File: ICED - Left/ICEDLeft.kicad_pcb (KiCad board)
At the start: 2 copper layers, 175.4 x 145 mm, 162 parts, among them P1 Conn_ARM_JTAG_SWD_10, P2 DX07S024XJ1R1100, P3 CONN_17, P4 692121130100, P5 RGB Out, Q1 TC1264, U1 MK20DX256VLH7, U2 IS31FL3737-QFLS4-TR, X1 CRYSTAL

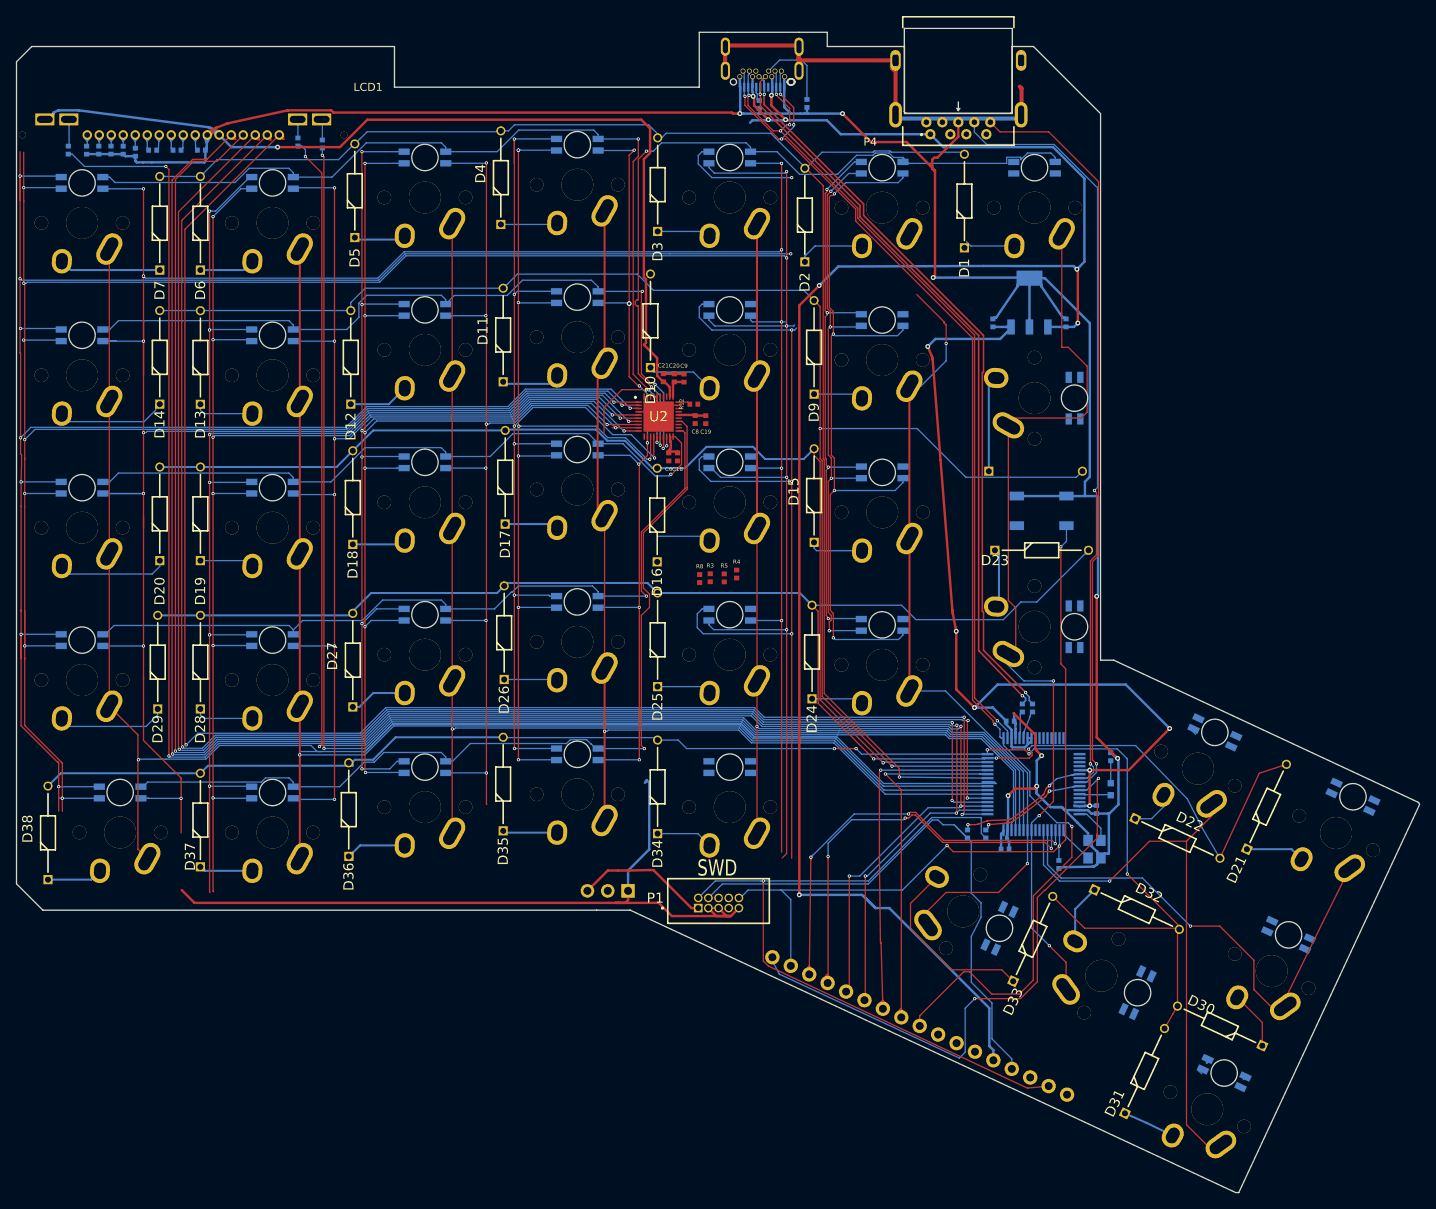
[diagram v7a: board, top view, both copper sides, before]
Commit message: Cleaned up DRC issues
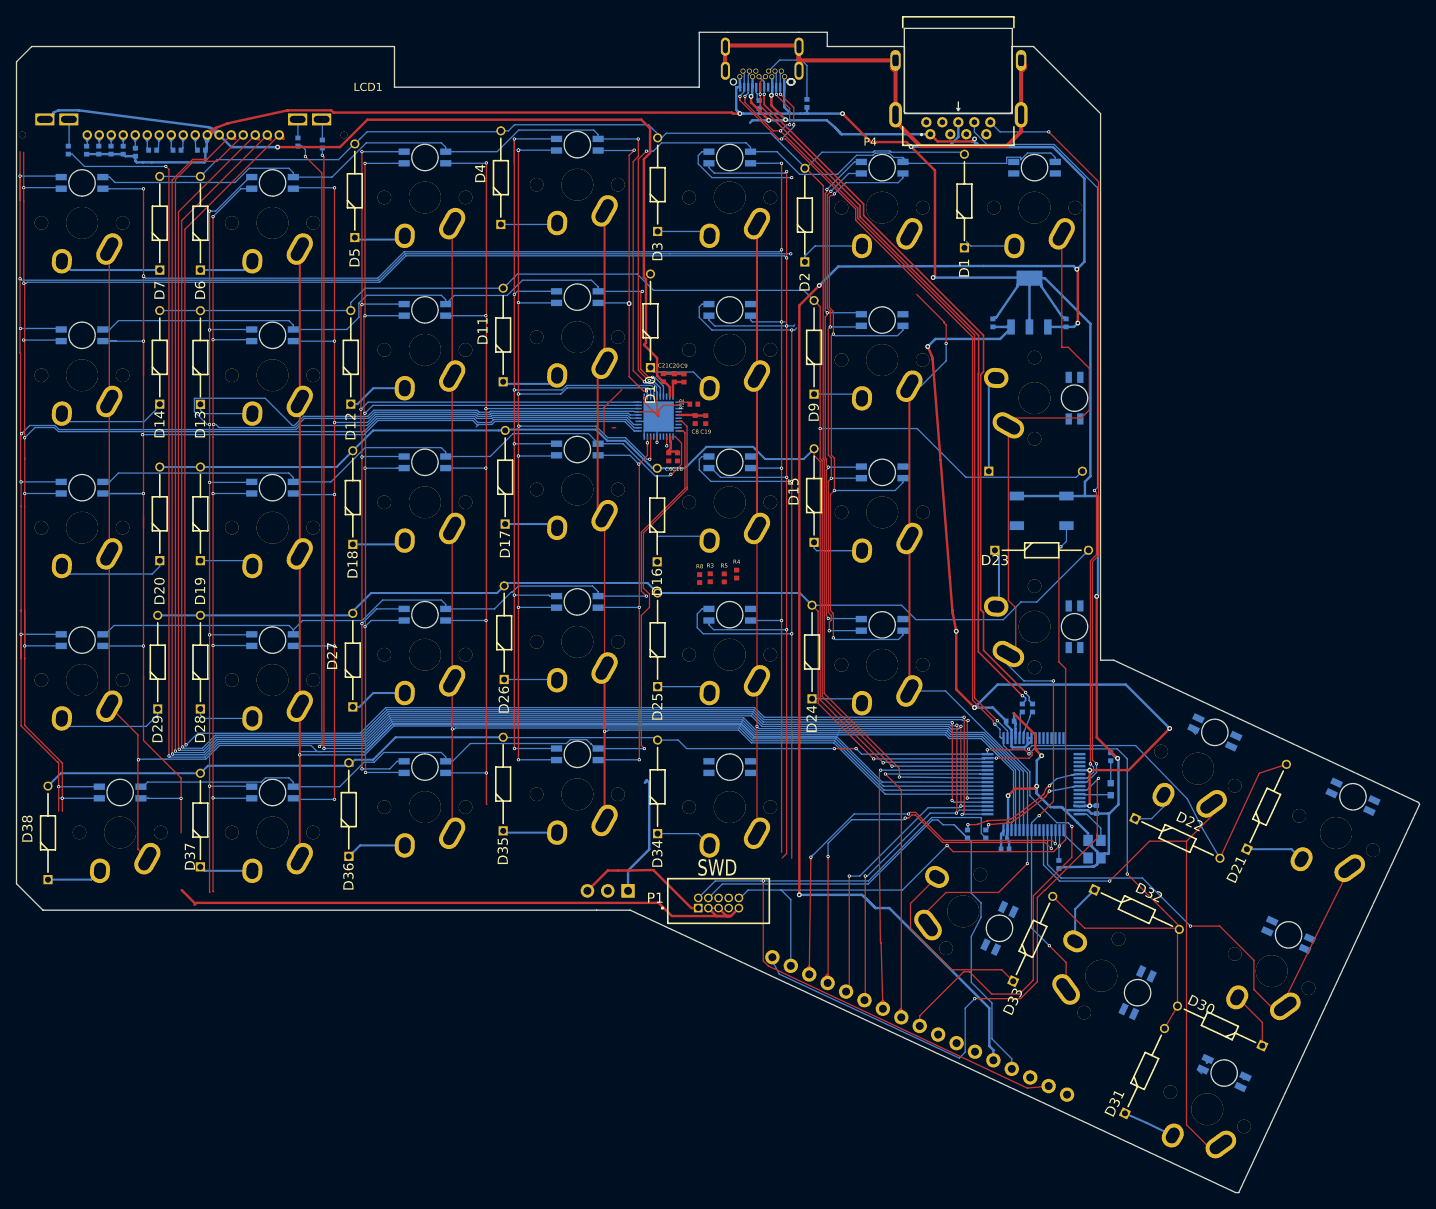
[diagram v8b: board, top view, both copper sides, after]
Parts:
- U2: moved to B.Cu
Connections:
- U1 pad 40: /Col7 -> (no net)
- U1 pad 55: (no net) -> /Col7
- U1 pad 56: (no net) -> /Col8
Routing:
- net /mcu/ledmatrix_2/Green4: track 122.1 -> 139.8 mm, vias 8 -> 9
- net /mcu/ledmatrix_2/GND: track 12.1 -> 21.9 mm
- net /GND: track 56.3 -> 64.3 mm
- net /mcu/ledmatrix_2/Row2A: track 97.2 -> 89.2 mm, vias 3 -> 2
- net /mcu/ledmatrix_2/Row1B: track 98.3 -> 90.9 mm, vias 3 -> 2
- net /mcu/ledmatrix_2/Red4: track 104.1 -> 98.7 mm
- net /mcu/ledmatrix_2/Row1A: track 113.3 -> 108.1 mm
- net /mcu/ledmatrix_2/Blue2: track 243.0 -> 248.1 mm, vias 11 -> 10
- net /mcu/ledmatrix_2/Blue4: track 129.9 -> 125.0 mm, vias 7 -> 6
- net /mcu/ledmatrix_2/Row5A: track 122.5 -> 119.5 mm
- net /mcu/ledmatrix_2/Blue3: track 142.1 -> 139.7 mm, vias 7 -> 6
- net /Col9: track 255.9 -> 253.7 mm
- net /mcu/ledmatrix_2/Red2: track 238.6 -> 236.5 mm, vias 11 -> 10
- net /mcu/ledmatrix_2/Green2: track 239.0 -> 237.0 mm, vias 11 -> 10
- net /mcu/ledmatrix_2/Red3: track 126.8 -> 124.8 mm, vias 7 -> 6
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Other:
- outline, holes or cut-outs redrawn
